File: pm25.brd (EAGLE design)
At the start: 47 x 22.9 mm, 12 parts, among them U2 CCS811B-JOPD500, U4 SI7021-A20-GM1R

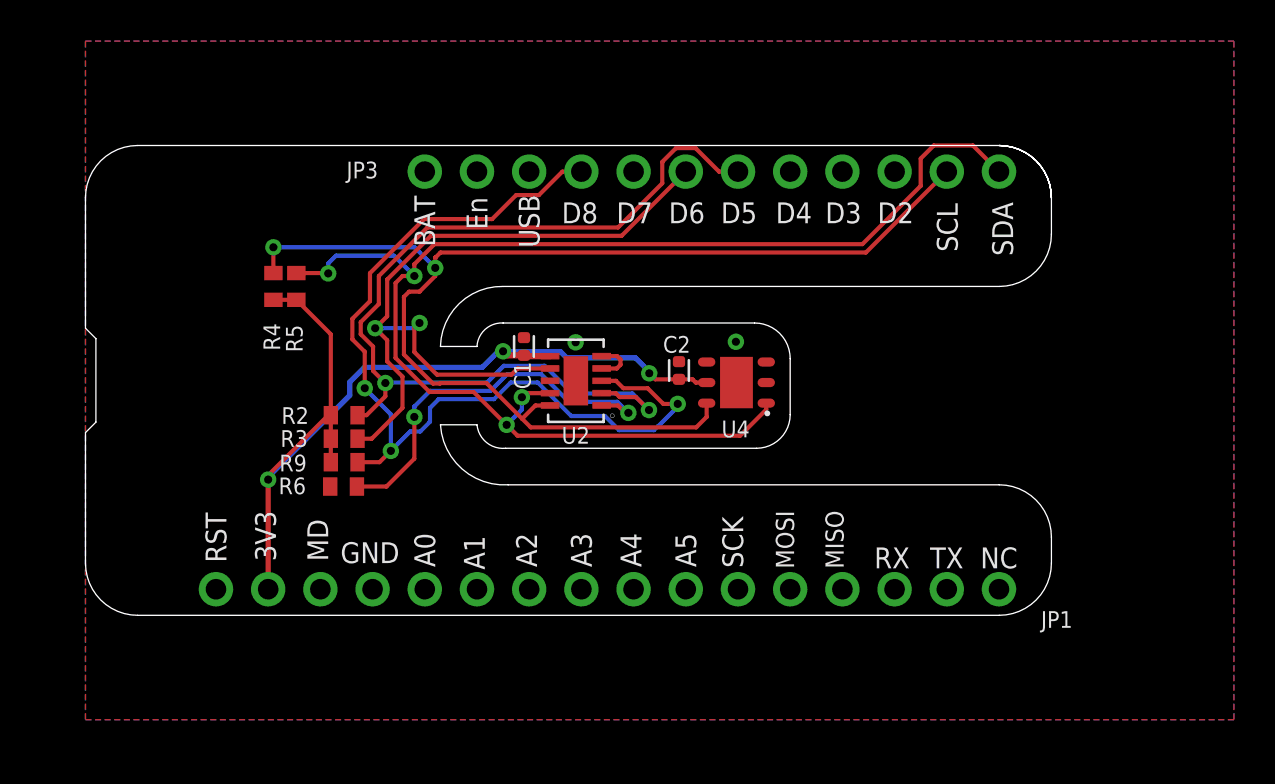
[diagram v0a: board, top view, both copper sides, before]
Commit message: rip up all traces outside of island
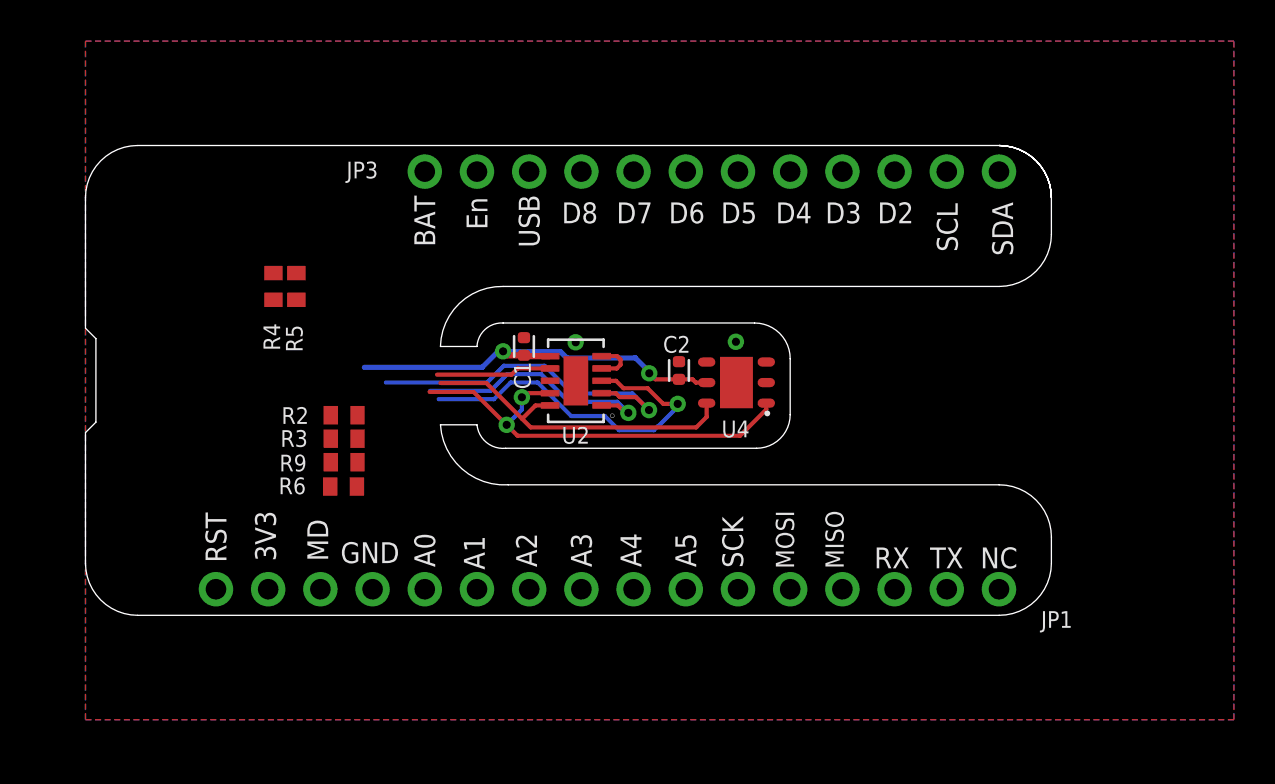
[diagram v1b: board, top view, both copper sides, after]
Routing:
- net SDA: track 67.8 -> 21.2 mm, vias 4 -> 2
- net SCL: track 60.6 -> 16.4 mm, vias 2 -> 0
- net D6: track 37.5 -> 5.63 mm, vias 2 -> 0
- net D5: track 46.3 -> 16.7 mm, vias 2 -> 1
- net D8: track 45.6 -> 17.9 mm, vias 3 -> 1
- net +3V3: track 47.0 -> 20.2 mm, vias 3 -> 2
- net N$4: track 19.2 -> 12.2 mm, vias 2 -> 1

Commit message: Move resistors to bottom and align
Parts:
- moved R2 2.43 mm to (10.2, 14.8), flipped to the bottom, turned to 0 degrees
- moved R3 2.43 mm to (10.2, 13.7), flipped to the bottom, turned to 0 degrees
- moved R6 2.43 mm to (10.2, 12.5), flipped to the bottom, turned to 0 degrees
- moved R9 2.40 mm to (10.2, 11.3), flipped to the bottom, turned to 180 degrees
- moved R5 1.38 mm to (10.2, 19.7), flipped to the bottom, turned to 0 degrees
- moved R4 1.05 mm to (10.2, 20.8), flipped to the bottom, turned to 0 degrees

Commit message: Huge reroute effort - not done yet
Also replace pours: Top=GND, Bottom=+3V3
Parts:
- moved R9 8.97 mm to (10.2, 20.3)
- moved R4 6.86 mm to (10.2, 14.0)
- moved R2 6.77 mm to (10.2, 21.6)
- moved R6 6.52 mm to (10.2, 19.1)
- moved R5 4.47 mm to (10.2, 15.2)
- moved R3 4.11 mm to (10.2, 17.8)
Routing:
- net SCL: track 16.4 -> 74.6 mm, vias 0 -> 2
- net SDA: track 21.2 -> 71.2 mm
- net D8: track 17.9 -> 60.3 mm, vias 1 -> 2
- net D6: track 5.63 -> 44.6 mm, vias 0 -> 2
- net D5: track 16.7 -> 45.0 mm, vias 1 -> 2
- net +3V3: track 20.0 -> 4.96 mm, vias 2 -> 1
- net N$4: track 12.2 -> 20.2 mm
- added copper zone on layer 16, net +3V3
- removed copper zone on layer 16, net GND

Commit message: Opened up the channel and improved the routing
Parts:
- moved R5 2.54 mm to (10.2, 12.7)
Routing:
- net SCL: track 74.6 -> 62.2 mm
- net D8: track 60.3 -> 51.0 mm, vias 2 -> 1
- net D6: track 44.6 -> 36.2 mm, vias 2 -> 1
- net N$4: track 20.2 -> 19.3 mm
- net D5: track 45.0 -> 44.2 mm
- net SDA: track 71.2 -> 70.4 mm
- net +3V3: track 4.96 -> 5.59 mm, vias 1 -> 2
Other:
- outline, holes or cut-outs redrawn

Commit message: routing done but pours barely connect
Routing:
- net D8: track 51.0 -> 40.6 mm, vias 1 -> 2
- net GND: track 0.00 -> 3.03 mm, vias 0 -> 1
- net SCL: track 62.2 -> 59.7 mm
- net SDA: track 70.4 -> 68.3 mm
- net D5: track 44.2 -> 45.2 mm, vias 2 -> 1
- net D6: track 36.2 -> 36.9 mm, vias 1 -> 2

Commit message: happy with the routing now
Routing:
- net D5: track 45.2 -> 44.0 mm, vias 1 -> 3
- net SDA: track 68.3 -> 69.0 mm, vias 2 -> 3
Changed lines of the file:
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@@
 <wire x1="25.959834375" y1="14.08903125" x2="25.272415625" y2="14.77645" width="0.2032" layer="16"/>
 <wire x1="24.13" y1="26.67" x2="24.13" y2="26.162" width="0.2032" layer="1"/>
-<wire x1="24.13" y1="26.162" x2="23.241" y2="25.273" width="0.2032" layer="1"/>
+<wire x1="24.13" y1="26.162" x2="22.86" y2="24.892" width="0.2032" layer="1"/>
 <wire x1="10.81" y1="19.05" x2="12.065" y2="19.05" width="0.2032" layer="16"/>
 <wire x1="12.065" y1="19.05" x2="14.859" y2="16.256" width="0.2032" layer="16"/>
@@
 <wire x1="12.065" y1="19.05" x2="12.0444625" y2="19.0294625" width="0.2032" layer="16"/>
 <via x="12.0444625" y="19.0294625" extent="1-16" drill="0.3937"/>
-<wire x1="12.0444625" y1="19.0294625" x2="18.288" y2="25.273" width="0.2032" layer="1"/>
-<wire x1="18.288" y1="25.273" x2="23.241" y2="25.273" width="0.2032" layer="1"/>
+<wire x1="12.0444625" y1="19.0294625" x2="17.907" y2="24.892" width="0.2032" layer="1"/>
+<wire x1="17.907" y1="24.892" x2="22.86" y2="24.892" width="0.2032" layer="1"/>
 </signal>
 <signal name="A0">
@@
 <wire x1="29.71800625" y1="14.22400625" x2="21.28519375" y2="14.22400625" width="0.2032" layer="1"/>
 <wire x1="41.91" y1="26.67" x2="41.91" y2="24.892" width="0.2032" layer="1"/>
-<wire x1="41.021" y1="24.003" x2="19.431" y2="24.003" width="0.2032" layer="1"/>
-<wire x1="41.91" y1="24.892" x2="41.021" y2="24.003" width="0.2032" layer="1"/>
+<wire x1="40.767" y1="23.749" x2="19.177" y2="23.749" width="0.2032" layer="1"/>
+<wire x1="41.91" y1="24.892" x2="40.767" y2="23.749" width="0.2032" layer="1"/>
 <wire x1="22.606" y1="15.2908" x2="21.45665" y2="15.2908" width="0.2032" layer="1"/>
 <wire x1="21.45665" y1="15.2908" x2="20.955" y2="14.78915" width="0.2032" layer="1"/>
@@
 <wire x1="21.28519375" y1="14.22400625" x2="20.955" y2="14.5542" width="0.2032" layer="1"/>
 <wire x1="20.955" y1="14.78915" x2="20.955" y2="14.5542" width="0.2032" layer="1"/>
-<wire x1="19.431" y1="24.003" x2="12.319" y2="16.891" width="0.2032" layer="1"/>
+<wire x1="19.177" y1="23.749" x2="12.319" y2="16.891" width="0.2032" layer="1"/>
 <wire x1="10.81" y1="13.97" x2="11.62915" y2="14.78915" width="0.2032" layer="16"/>
 <wire x1="11.62915" y1="14.78915" x2="12.319" y2="14.78915" width="0.2032" layer="16"/>
@@
 <contactref element="U2" pad="9"/>
 <wire x1="33.126" y1="15.4048" x2="33.126" y2="15.092" width="0.2032" layer="1"/>
-<wire x1="33.126" y1="15.092" x2="31.75" y2="13.716" width="0.2032" layer="1"/>
 <contactref element="R5" pad="1"/>
-<wire x1="44.45" y1="26.67" x2="44.45" y2="23.749" width="0.2032" layer="1"/>
+<wire x1="44.45" y1="26.67" x2="44.45" y2="24.765" width="0.2032" layer="1"/>
 <wire x1="22.606" y1="15.8908" x2="22.5902" y2="15.875" width="0.2032" layer="1"/>
 <wire x1="20.955" y1="15.875" x2="22.5902" y2="15.875" width="0.2032" layer="1"/>
-<via x="18.288" y="13.716" extent="1-16" drill="0.3937"/>
+<via x="18.288" y="13.589" extent="1-16" drill="0.3937"/>
 <wire x1="10.81" y1="12.7" x2="12.334" y2="12.7" width="0.2032" layer="16"/>
 <wire x1="13.35" y1="13.716" x2="12.334" y2="12.7" width="0.2032" layer="16"/>
-<wire x1="18.288" y1="13.716" x2="13.35" y2="13.716" width="0.2032" layer="16"/>
+<wire x1="18.288" y1="13.589" x2="13.477" y2="13.589" width="0.2032" layer="16"/>
+<wire x1="13.477" y1="13.589" x2="13.35" y2="13.716" width="0.2032" layer="16"/>
 <via x="13.35" y="13.716" extent="1-16" drill="0.3937"/>
-<wire x1="43.942" y1="23.241" x2="19.812" y2="23.241" width="0.2032" layer="1"/>
+<wire x1="42.926" y1="23.241" x2="19.812" y2="23.241" width="0.2032" layer="1"/>
 <wire x1="19.812" y1="23.241" x2="13.335" y2="16.764" width="0.2032" layer="1"/>
 <wire x1="13.335" y1="16.764" x2="13.335" y2="13.731" width="0.2032" layer="1"/>
 <wire x1="13.35" y1="13.716" x2="13.335" y2="13.731" width="0.2032" layer="1"/>
-<wire x1="44.45" y1="23.749" x2="43.942" y2="23.241" width="0.2032" layer="1"/>
-<wire x1="18.796" y1="13.716" x2="18.288" y2="13.716" width="0.2032" layer="1"/>
-<wire x1="18.796" y1="13.716" x2="18.923" y2="13.843" width="0.2032" layer="1"/>
-<wire x1="18.923" y1="13.843" x2="20.955" y2="15.875" width="0.2032" layer="1"/>
-<wire x1="31.75" y1="13.716" x2="18.796" y2="13.716" width="0.2032" layer="1"/>
+<wire x1="44.45" y1="24.765" x2="42.926" y2="23.241" width="0.2032" layer="1"/>
+<wire x1="18.923" y1="14.224" x2="18.288" y2="13.589" width="0.2032" layer="1"/>
+<wire x1="18.923" y1="14.224" x2="19.304" y2="14.224" width="0.2032" layer="1"/>
+<wire x1="19.304" y1="14.224" x2="20.955" y2="15.875" width="0.2032" layer="1"/>
+<wire x1="33.126" y1="15.4048" x2="33.126" y2="14.584" width="0.2032" layer="1"/>
+<wire x1="33.126" y1="14.584" x2="32.893" y2="14.351" width="0.2032" layer="1"/>
+<via x="32.893" y="14.351" extent="1-16" drill="0.3937"/>
+<wire x1="32.893" y1="14.351" x2="32.131" y2="13.589" width="0.2032" layer="16"/>
+<wire x1="32.131" y1="13.589" x2="18.288" y2="13.589" width="0.2032" layer="16"/>
 </signal>
 <signal name="D4">
@@
 <wire x1="10.81" y1="16.368" x2="10.81" y2="17.78" width="0.2032" layer="16"/>
 <via x="10.81" y="16.368" extent="1-16" drill="0.3937"/>
-<wire x1="19.08" y1="24.638" x2="10.81" y2="16.368" width="0.2032" layer="1"/>
-<wire x1="29.21" y1="26.67" x2="27.178" y2="24.638" width="0.2032" layer="1"/>
-<wire x1="27.178" y1="24.638" x2="19.08" y2="24.638" width="0.2032" layer="1"/>
+<wire x1="18.826" y1="24.384" x2="10.81" y2="16.368" width="0.2032" layer="1"/>
+<wire x1="29.21" y1="26.67" x2="26.924" y2="24.384" width="0.2032" layer="1"/>
+<wire x1="26.924" y1="24.384" x2="18.826" y2="24.384" width="0.2032" layer="1"/>
 </signal>
 <signal name="D5">
@@
 <wire x1="26.6119625" y1="15.875" x2="23.6887375" y2="15.875" width="0.2032" layer="16"/>
 <wire x1="23.6887375" y1="15.875" x2="22.2917375" y2="17.272" width="0.2032" layer="16"/>
-<wire x1="22.2917375" y1="17.272" x2="15.636" y2="17.272" width="0.2032" layer="16"/>
-<wire x1="31.75" y1="26.67" x2="29.083" y2="24.003" width="0.2032" layer="16"/>
-<wire x1="10.81" y1="21.59" x2="11.318" y2="21.59" width="0.2032" layer="16"/>
-<wire x1="15.636" y1="17.272" x2="11.8185" y2="21.0895" width="0.2032" layer="16"/>
-<wire x1="11.8185" y1="21.0895" x2="11.3105" y2="21.5975" width="0.2032" layer="16"/>
-<wire x1="29.083" y1="24.003" x2="13.716" y2="24.003" width="0.2032" layer="16"/>
-<wire x1="13.716" y1="24.003" x2="11.3105" y2="21.5975" width="0.2032" layer="16"/>
-<wire x1="11.318" y1="21.59" x2="11.8185" y2="21.0895" width="0.2032" layer="16"/>
+<wire x1="22.2917375" y1="17.272" x2="16.525" y2="17.272" width="0.2032" layer="16"/>
+<wire x1="31.75" y1="26.67" x2="29.972" y2="24.892" width="0.2032" layer="16"/>
+<wire x1="10.81" y1="21.59" x2="12.207" y2="21.59" width="0.2032" layer="16"/>
+<wire x1="16.525" y1="17.272" x2="12.4535" y2="21.3435" width="0.2032" layer="16"/>
+<wire x1="12.4535" y1="21.3435" x2="12.207" y2="21.59" width="0.2032" layer="16"/>
+<wire x1="29.972" y1="24.892" x2="15.367" y2="24.892" width="0.2032" layer="16"/>
+<wire x1="12.207" y1="21.59" x2="12.4535" y2="21.3435" width="0.2032" layer="16"/>
+<via x="12.207" y="21.59" extent="1-16" drill="0.3937"/>
+<wire x1="12.207" y1="21.59" x2="12.207" y2="21.605" width="0.2032" layer="1"/>
+<wire x1="15.367" y1="24.765" x2="15.367" y2="24.892" width="0.2032" layer="1"/>
+<wire x1="15.367" y1="24.765" x2="12.207" y2="21.605" width="0.2032" layer="1"/>
+<via x="15.367" y="24.892" extent="1-16" drill="0.3937"/>
 </signal>
 <signal name="TX">

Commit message: rename the parts sequentially
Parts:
- removed R9: 100k, wolff-den:R0402
- removed U4: SI7021-A20-GM1R, wolff-den:SON100P300X300X80-7N
- added R1: 20k, wolff-den:R0402
- added U1: CCS811B-JOPD500, wolff-den:SON60P400X270X110-11N
- R2: value 100k -> 20k
- R4, R5: value 20k -> 100k
- U2: value CCS811B-JOPD500 -> SI7021-A20-GM1R; device wolff-den:SON60P400X270X110-11N -> wolff-den:SON100P300X300X80-7N
- moved U2 7.82 mm to (31.7, 16.4)
- moved R5 7.62 mm to (10.2, 20.3), turned to 180 degrees
- moved R2 7.62 mm to (10.2, 14.0)
- moved R4 5.08 mm to (10.2, 19.1)
- moved R6 2.54 mm to (10.2, 21.6)
- renumbered JP3 to JP2
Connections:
- net +3V3: now also R1.2, U1.6, U2.5; no longer R5.2, U2.6, U4.5
- net D5: now also R6.1, U1.2; no longer R2.1, U2.2
- net D6: now also U1.7; no longer U2.7
- net D8: now also R4.1, U1.3; no longer R6.1, U2.3
- net GND: now also R5.1, U1.11, U2.2, U2.7; no longer R9.1, U2.11, U4.2, U4.7
- net N$4: now also R5.2, U1.1; no longer R9.2, U2.1
- net N$5: now also U1.4, U1.5; no longer U2.4, U2.5
- net SCL: now also R2.1, U1.10, U2.6; no longer R4.1, U2.10, U4.6
- net SDA: now also R1.1, U1.9, U2.1; no longer R5.1, U2.9, U4.1
